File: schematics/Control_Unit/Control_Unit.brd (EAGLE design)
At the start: 58.4 x 65.4 mm, 144 parts, among them IC1 74HC174N, IC10 74HC74N, IC101 74HCT08N, IC103 74HC373N, IC104 74HCT08N, IC108 74HCT32N, IC11 74HC74N, IC110 74HCT32N, IC12 74AC08N, IC124 74HCT32N, IC125 74HCT08N, IC126 74AC157N, IC127 74HCT08N, IC128 74AC08N, IC129 74AC08N, IC13 74AC08N, IC130 74HCT04N, IC14 74HC74N, IC15 74HC74N, IC16 74AC08N, IC164 74HC174N, IC165 74HC174N, IC166 74HC174N, IC167 74HC174N, IC168 74HCT32N, IC169 74HCT32N, IC17 74HCT32N, IC172 74HCT32N, IC173 74HCT32N, IC174 74HCT32N, IC175 74HC193N, IC176 74HC193N, IC177 74HC193N, IC178 74HC193N, IC179 74HC193N, IC18 74AC08N, IC180 74HC193N, IC181 74HC193N, IC182 74HC193N, IC19 74AC08N, IC190 74HCT32N, IC191 74HCT32N, IC2 74HC174N, IC20 74AC08N, IC21 74AC08N, IC22 74HCT32N, IC23 74HCT08N, IC24 74HCT08N, IC25 74HCT32N, IC26 74HCT08N, IC27 74HCT08N, IC28 74HCT08N, IC29 74HCT08N, IC3 74HC151N, IC30 74HCT08N, IC31 74HCT04N, IC32 74HCT32N, IC33 74HCT32N, IC34 74HCT08N, IC35 74HCT04N, IC36 CY62256LL-PC, IC37 74HCT04N, IC38 74HCT08N, IC39 74HCT08N, IC4 74HC174N, IC40 74HCT32N, IC41 74HCT08N, IC42 74HC373N, IC43 74HCT04N, IC44 74HCT04N, IC45 74HCT04N, IC46 74ACT157N, IC47 74HCT04N, IC48 74HCT04N, IC49 74AC86N, IC5 74HC174N, IC50 74HC174N, IC51 74HCT32N, IC52 74HCT32N, IC53 74HCT32N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

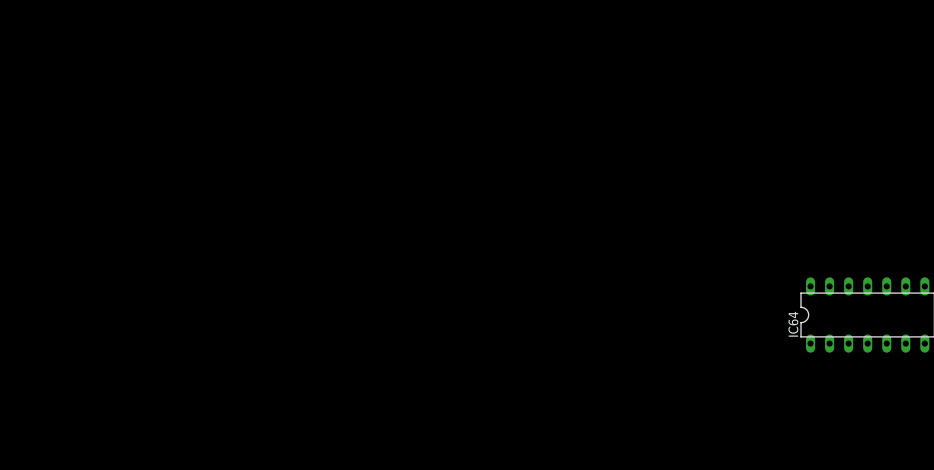
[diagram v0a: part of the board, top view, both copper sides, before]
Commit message: add second byte load of instruction fetch.
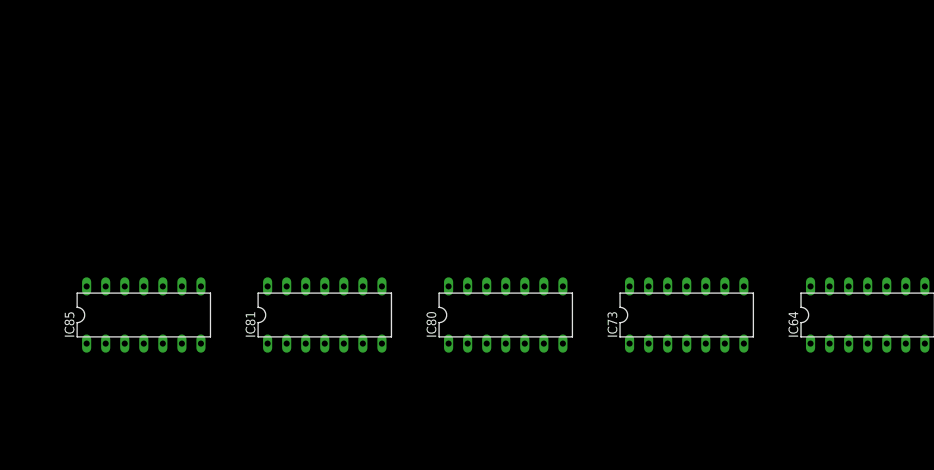
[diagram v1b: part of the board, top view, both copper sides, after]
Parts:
- added IC73, IC81: 74HCT08N, 74xx-eu:DIL14
- added IC80, IC85: 74HCT32N, 74xx-eu:DIL14
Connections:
- removed net IR_HIGH_LOAD_INPUT: IC4.9, IC5.9
- new net CLR_NOT_OE/CLR_NOT_CS_CYCL_2: IC80.11, IC85.2
- new net IR_LOAD_INPUT: IC4.9, IC5.9, IC80.12, IC81.11
- new net N$195: IC73.11, IC80.13
- new net N$200: IC63.13, IC85.3
- new net TWO_BYTE_CMD: IC73.12, IC81.13
- net CLR_NOT_CS_LDR: now also IC85.1; no longer IC63.13
- net CYCL_3: now also IC73.13
- net CYCL_4: now also IC81.12
- net GND: now also IC73.7, IC80.7, IC81.7, IC85.7
- net VCC: now also IC73.14, IC80.14, IC81.14, IC85.14
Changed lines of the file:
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@@
 <element name="IC31" library="74xx-eu" package="DIL14" value="74HCT04N" x="-63.1825" y="3.175"/>
 <element name="IC64" library="74xx-eu" package="DIL14" value="74HCT08N" x="-69.215" y="3.175"/>
+<element name="IC73" library="74xx-eu" package="DIL14" value="74HCT08N" x="-75.2475" y="3.175"/>
+<element name="IC80" library="74xx-eu" package="DIL14" value="74HCT32N" x="-81.28" y="3.175"/>
+<element name="IC81" library="74xx-eu" package="DIL14" value="74HCT08N" x="-87.3125" y="3.175"/>
+<element name="IC85" library="74xx-eu" package="DIL14" value="74HCT32N" x="-93.345" y="3.175"/>
 </elements>
 <signals>
@@
 <contactref element="IC31" pad="7"/>
 <contactref element="IC64" pad="7"/>
+<contactref element="IC73" pad="7"/>
+<contactref element="IC80" pad="7"/>
+<contactref element="IC81" pad="7"/>
+<contactref element="IC85" pad="7"/>
 <wire x1="52.3875" y1="58.1025" x2="49.8575" y2="63.5" width="0" layer="19" extent="1-1"/>
 <wire x1="51.435" y1="53.975" x2="52.3875" y2="58.1025" width="0" layer="19" extent="1-1"/>
@@
 <wire x1="-61.2775" y1="2.2225" x2="-49.2125" y2="2.2225" width="0" layer="19" extent="1-1"/>
 <wire x1="-67.31" y1="2.2225" x2="-61.2775" y2="2.2225" width="0" layer="19" extent="1-1"/>
+<wire x1="-73.3425" y1="2.2225" x2="-67.31" y2="2.2225" width="0" layer="19" extent="1-1"/>
+<wire x1="-79.375" y1="2.2225" x2="-73.3425" y2="2.2225" width="0" layer="19" extent="1-1"/>
+<wire x1="-85.4075" y1="2.2225" x2="-79.375" y2="2.2225" width="0" layer="19" extent="1-1"/>
+<wire x1="-91.44" y1="2.2225" x2="-85.4075" y2="2.2225" width="0" layer="19" extent="1-1"/>
 </signal>
 <signal name="VCC">
@@
 <contactref element="IC31" pad="14"/>
 <contactref element="IC64" pad="14"/>
+<contactref element="IC73" pad="14"/>
+<contactref element="IC80" pad="14"/>
+<contactref element="IC81" pad="14"/>
+<contactref element="IC85" pad="14"/>
 <wire x1="46.6725" y1="60.0075" x2="51.1075" y2="63.5" width="0" layer="19" extent="1-1"/>
 <wire x1="46.99" y1="55.88" x2="46.6725" y2="60.0075" width="0" layer="19" extent="1-1"/>
@@
 <wire x1="-65.0875" y1="4.1275" x2="-53.0225" y2="4.1275" width="0" layer="19" extent="1-1"/>
 <wire x1="-71.12" y1="4.1275" x2="-65.0875" y2="4.1275" width="0" layer="19" extent="1-1"/>
+<wire x1="-77.1525" y1="4.1275" x2="-71.12" y2="4.1275" width="0" layer="19" extent="1-1"/>
+<wire x1="-83.185" y1="4.1275" x2="-77.1525" y2="4.1275" width="0" layer="19" extent="1-1"/>
+<wire x1="-89.2175" y1="4.1275" x2="-83.185" y2="4.1275" width="0" layer="19" extent="1-1"/>
+<wire x1="-95.25" y1="4.1275" x2="-89.2175" y2="4.1275" width="0" layer="19" extent="1-1"/>
 </signal>
 <signal name="CLR_NOT_OE/CLR_NOT_CS_CYCL_0">
@@
 <contactref element="IC11" pad="5"/>
 <contactref element="IC11" pad="12"/>
-<wire x1="9.2075" y1="53.0225" x2="10.4775" y2="51.1175" width="0" layer="19" extent="1-1"/>
+<contactref element="IC73" pad="13"/>
+<wire x1="9.2075" y1="53.0225" x2="-76.5175" y2="4.1275" width="0" layer="19" extent="1-1"/>
+<wire x1="10.4775" y1="51.1175" x2="9.2075" y2="53.0225" width="0" layer="19" extent="1-1"/>
 </signal>
 <signal name="CYCL_5">
@@
 <contactref element="IC14" pad="2"/>
 <contactref element="IC11" pad="9"/>
-<wire x1="11.1125" y1="53.0225" x2="13.6525" y2="51.1175" width="0" layer="19" extent="1-1"/>
+<contactref element="IC81" pad="12"/>
+<wire x1="11.1125" y1="53.0225" x2="-87.9475" y2="4.1275" width="0" layer="19" extent="1-1"/>
+<wire x1="13.6525" y1="51.1175" x2="11.1125" y2="53.0225" width="0" layer="19" extent="1-1"/>
 </signal>
 <signal name="OPCODE_2">
@@
 <wire x1="5.3975" y1="41.5925" x2="25.7175" y2="24.4475" width="0" layer="19" extent="1-1"/>
 </signal>
-<signal name="IR_HIGH_LOAD_INPUT">
+<signal name="IR_LOAD_INPUT">
 <contactref element="IC4" pad="9"/>
 <contactref element="IC5" pad="9"/>
-<wire x1="13.0175" y1="37.7825" x2="18.7325" y2="37.7825" width="0" layer="19" extent="1-1"/>
+<contactref element="IC81" pad="11"/>
+<contactref element="IC80" pad="12"/>
+<wire x1="-81.915" y1="4.1275" x2="-87.3125" y2="4.1275" width="0" layer="19" extent="1-1"/>
+<wire x1="13.0175" y1="37.7825" x2="-81.915" y2="4.1275" width="0" layer="19" extent="1-1"/>
+<wire x1="18.7325" y1="37.7825" x2="13.0175" y2="37.7825" width="0" layer="19" extent="1-1"/>
 </signal>
 <signal name="REG_0_LOAD_INPUT">
@@
 </signal>
 <signal name="CLR_NOT_CS_LDR">
-<contactref element="IC63" pad="13"/>
 <contactref element="IC173" pad="1"/>
 <contactref element="IC173" pad="6"/>
+<contactref element="IC85" pad="1"/>
 <wire x1="38.4175" y1="58.7375" x2="41.5925" y2="58.7375" width="0" layer="19" extent="1-1"/>
-<wire x1="33.9725" y1="56.8325" x2="38.4175" y2="58.7375" width="0" layer="19" extent="1-1"/>
+<wire x1="-95.25" y1="2.2225" x2="38.4175" y2="58.7375" width="0" layer="19" extent="1-1"/>
 </signal>
 <signal name="CLR_NOT_CS_STR">
@@
 </signal>
 <signal name="N$126">
-<contactref element="IC17" pad="3"/>
 <contactref element="IC63" pad="12"/>
+<contactref element="IC17" pad="3"/>
 <wire x1="-3.4925" y1="2.2225" x2="34.6075" y2="56.8325" width="0" layer="19" extent="1-1"/>
 </signal>
@@
 <contactref element="IC20" pad="11"/>
 </signal>
+<signal name="TWO_BYTE_CMD">
+<contactref element="IC81" pad="13"/>
+<contactref element="IC73" pad="12"/>
+<wire x1="-75.8825" y1="4.1275" x2="-88.5825" y2="4.1275" width="0" layer="19" extent="1-1"/>
+</signal>
+<signal name="N$195">
+<contactref element="IC73" pad="11"/>
+<contactref element="IC80" pad="13"/>
+<wire x1="-75.2475" y1="4.1275" x2="-82.55" y2="4.1275" width="0" layer="19" extent="1-1"/>
+</signal>
+<signal name="CLR_NOT_OE/CLR_NOT_CS_CYCL_2">
+<contactref element="IC80" pad="11"/>
+<contactref element="IC85" pad="2"/>
+<wire x1="-81.28" y1="4.1275" x2="-94.615" y2="2.2225" width="0" layer="19" extent="1-1"/>
+</signal>
+<signal name="N$200">
+<contactref element="IC63" pad="13"/>
+<contactref element="IC85" pad="3"/>
+<wire x1="33.9725" y1="56.8325" x2="-93.98" y2="2.2225" width="0" layer="19" extent="1-1"/>
+</signal>
 </signals>

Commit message: reorder arguments. decoding is now easier
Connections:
- net INPUT_REG==OUTPUT_REG renamed INPUT_REG_IS_NOT_OUTPUT_REG
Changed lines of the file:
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@@
 <wire x1="9.2075" y1="43.4975" x2="3.4925" y2="49.2125" width="0" layer="19" extent="1-1"/>
 </signal>
-<signal name="INPUT_REG==OUTPUT_REG">
+<signal name="INPUT_REG_IS_NOT_OUTPUT_REG">
 <contactref element="IC168" pad="11"/>
 <contactref element="IC76" pad="1"/>

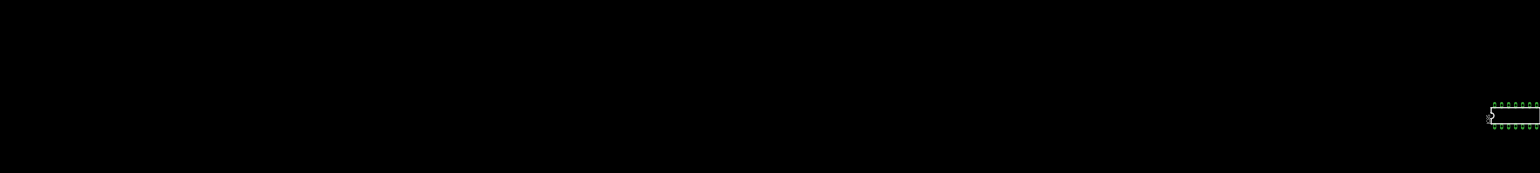
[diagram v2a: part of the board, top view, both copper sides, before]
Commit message: add two byte cmd decoder
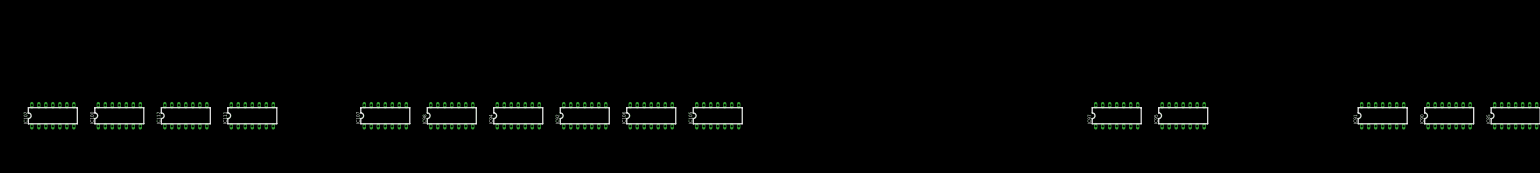
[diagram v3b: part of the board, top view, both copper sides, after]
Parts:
- added IC100, IC105, IC106, IC111, IC112, IC92, IC94, IC97, IC98: 74HCT32N, 74xx-eu:DIL14
- added IC102, IC107, IC90: 74HCT04N, 74xx-eu:DIL14
- added IC91, IC95: 74HCT08N, 74xx-eu:DIL14
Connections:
- removed net N$112: IC21.3, IC27.2, IC27.5, IC28.2
- removed net N$129: IC21.8, IC23.10, IC23.2, IC23.5
- removed net N$148: IC21.11, IC23.13, IC24.10, IC24.2, IC24.5
- removed net N$194: IC20.11
- new net LDR: IC112.12, IC21.3, IC27.2, IC27.5, IC28.2
- new net N$201: IC91.11, IC97.12
- new net N$203: IC95.11, IC97.13
- new net N$205: IC90.8, IC91.12
- new net N$206: IC102.8, IC91.13
- new net N$207: IC107.9, IC98.11
- new net N$213: IC94.11, IC98.13
- new net N$217: IC92.11, IC98.12
- new net N$218: IC100.13, IC105.11, IC95.12
- new net N$220: IC105.12, IC106.11
- new net N$227: IC107.8, IC95.13
- new net N$230: IC111.12, IC112.11
- new net POP: IC111.13, IC21.11, IC23.13, IC24.10, IC24.2, IC24.5
- new net PTR_ADD: IC101.10, IC104.10, IC104.13, IC104.2, IC106.13, IC124.4, IC127.5, IC20.6
- new net PUSH: IC105.13, IC21.8, IC23.10, IC23.2, IC23.5
- new net SAVE_LR/RET: IC112.13, IC20.11
- new net STR: IC106.12, IC21.6, IC27.10, IC27.13
- net GND: now also IC100.7, IC102.7, IC105.7, IC106.7, IC107.7, IC111.7, IC112.7, IC90.7, IC91.7, IC92.7, IC94.7, IC95.7, IC97.7, IC98.7
- net INPUT_REG_IS_NOT_OUTPUT_REG: now also IC90.9
- net N$13: now also IC100.12, IC111.11; no longer IC21.6, IC27.10, IC27.13
- net N$7: now also IC100.11, IC102.9; no longer IC101.10, IC104.10, IC104.13, IC104.2, IC124.4, IC127.5, IC20.6
- net OPCODE_4: now also IC92.12
- net OPCODE_5: now also IC94.12
- net OPCODE_6: now also IC92.13
- net OPCODE_7: now also IC94.13
- net TWO_BYTE_CMD: now also IC97.11
- net VCC: now also IC100.14, IC102.14, IC105.14, IC106.14, IC107.14, IC111.14, IC112.14, IC90.14, IC91.14, IC92.14, IC94.14, IC95.14, IC97.14, IC98.14

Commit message: implement SAVE_LR/RET structure. LR register needs to be added.
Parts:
- removed IC102: 74HCT04N, 74xx-eu:DIL14
- removed IC105, IC106, IC111, IC174, IC92, IC94, IC97, IC98: 74HCT32N, 74xx-eu:DIL14
- removed IC95: 74HCT08N, 74xx-eu:DIL14
- added IC109: 74HCT08N, 74xx-eu:DIL14
- added IC117: 74HC74N, 74xx-eu:DIL14
- IC29: value 74HCT08N -> 74HCT32N
- IC31, IC48: value 74HCT04N -> 74HCT32N
- IC51, IC53: value 74HCT32N -> 74HCT08N
- IC90: value 74HCT04N -> 74HCT08N
- moved IC29 302.2 mm to (-268.3, 3.17)
- moved IC48 265.4 mm to (-280.4, 3.17)
- moved IC51 265.4 mm to (-286.4, 3.17)
- moved IC53 265.4 mm to (-292.4, 3.17)
- moved IC70 247.3 mm to (-298.4, 3.17)
- moved IC73 229.2 mm to (-304.5, 3.17)
- moved IC85 223.2 mm to (-316.5, 3.17)
- moved IC81 223.2 mm to (-310.5, 3.17)
- moved IC90 223.2 mm to (-322.6, 3.17)
- moved IC31 211.1 mm to (-274.3, 3.17)
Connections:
- net CYCL6 renamed CYCL_6
- net TABLE_B_INPUT_BR_HIGH renamed TABLE_B_INPUT_PTR_HIGH
- new net CYCL_0: IC10.12, IC10.5, IC80.5
- new net CYCL_10: IC10.2, IC117.9
- new net CYCL_8: IC117.2, IC15.9
- new net CYCL_9: IC117.12, IC117.5
- new net N$112: IC109.3, IC29.2
- new net N$129: IC109.10, IC130.10
- new net N$194: IC109.11, IC109.2, IC73.2, IC81.5, IC90.5
- new net N$219: IC109.5, IC109.8, IC51.2, IC53.5, IC70.5
- new net N$223: IC109.6, IC31.2
- new net N$224: IC85.1, IC90.6
- new net N$225: IC31.3
- new net N$226: IC48.2, IC53.6
- new net N$228: IC48.1, IC70.6
- new net N$229: IC29.1, IC73.3
- new net N$231: IC48.3
- new net N$232: IC85.3
- new net N$233: IC81.6, IC85.2
- new net WRITE_LR_DBUS_SAVE_LR: IC29.3
- net CLR_NOT_CS_LDR: now also IC17.4; no longer IC85.1
- net CLR_NOT_OE/CLR_NOT_CS_CYCL_0: now also IC80.6; no longer IC51.11
- net CLR_NOT_OE/CLR_NOT_CS_CYCL_2: now also IC17.5; no longer IC85.2
- net CYCL_3: now also IC91.5; no longer IC73.13
- net CYCL_4: now also IC91.1; no longer IC81.12
- net CYCL_7: now also IC15.12; no longer IC10.2
- net GND: now also IC109.7, IC117.7; no longer IC102.7, IC105.7, IC106.7, IC111.7, IC174.7, IC92.7, IC94.7, IC95.7, IC97.7, IC98.7
- net INPUT_REG_IS_NOT_OUTPUT_REG: now also IC107.11; no longer IC90.9
- net IR_LOAD_INPUT: now also IC91.3; no longer IC81.11
- net N$100: now also IC99.11; no longer IC53.3
- net N$118: now also IC124.12; no longer IC174.4
- net N$13: now also IC112.3; no longer IC111.11
- net N$132: now also IC125.6; no longer IC70.8
- net N$149: now also IC125.13, IC130.4; no longer IC29.10, IC31.2
- net N$15: now also IC125.11; no longer IC29.8
- net N$163: now also IC31.1, IC51.3; no longer IC10.12, IC10.5, IC51.13
- net N$168: now also IC99.13; no longer IC53.2
- net N$195: now also IC91.6; no longer IC73.11
- net N$197: now also IC124.11; no longer IC174.6
- net N$200: now also IC17.6; no longer IC85.3
- net N$201: now also IC80.1; no longer IC97.12
- net N$203: now also IC80.2, IC91.8; no longer IC95.11, IC97.13
- net N$205: now also IC107.10; no longer IC90.8
- net N$206: now also IC107.2; no longer IC102.8
- net N$207: now also IC100.8; no longer IC98.11
- net N$213: now also IC100.10, IC100.3; no longer IC94.11, IC98.13
- net N$217: now also IC100.6, IC100.9; no longer IC92.11, IC98.12
- net N$218: now also IC112.8, IC91.9; no longer IC105.11, IC95.12
- net N$22: now also IC125.5, IC130.3; no longer IC31.1, IC70.10
- net N$220: now also IC112.6, IC112.9; no longer IC105.12, IC106.11
- net N$227: now also IC91.10; no longer IC95.13
- net N$230: now also IC112.1; no longer IC111.12
- net N$31: now also IC37.1; no longer IC48.13
- net N$34: now also IC124.13; no longer IC174.5
- net N$69: now also IC37.2; no longer IC48.12
- net N$7: now also IC107.1; no longer IC102.9
- net N$82: now also IC125.12, IC125.4; no longer IC29.9, IC70.9
- net OPCODE_4: now also IC100.4; no longer IC92.12
- net OPCODE_5: now also IC100.1, IC109.12, IC130.11; no longer IC94.12
- net OPCODE_6: now also IC100.5; no longer IC92.13
- net OPCODE_7: now also IC100.2; no longer IC94.13
- net OPCODE_LOAD_INPUT: now also IC80.4; no longer IC51.12
- net PC_COUNT_UP_FETCH1: now also IC99.12; no longer IC53.1
- net POP: now also IC112.2; no longer IC111.13
- net PTR_ADD: now also IC112.5; no longer IC106.13
- net PUSH: now also IC112.10; no longer IC105.13
- net RING_CNTR_CLOCK: now also IC117.11, IC117.3, IC15.11
- net RING_CNTR_CLR: now also IC117.1, IC117.13, IC15.13
- net SAVE_LR/RET: now also IC109.13, IC109.9
- net STATE_1: now also IC109.1, IC109.4
- net STATE_2: now also IC51.1, IC73.1
- net STATE_3: now also IC53.4, IC81.4
- net STATE_4: now also IC70.4, IC90.4
- net STR: now also IC112.4; no longer IC106.12
- net TWO_BYTE_CMD: now also IC80.3, IC91.2, IC91.4; no longer IC73.12, IC81.13, IC97.11
- net VCC: now also IC109.14, IC117.14; no longer IC102.14, IC105.14, IC106.14, IC111.14, IC174.14, IC92.14, IC94.14, IC95.14, IC97.14, IC98.14

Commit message: add LR register. All instructions are now implemented.
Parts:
- added IC102, IC105, IC106, IC111, IC113, IC114, IC115, IC98: 74HC151N, 74xx-eu:DIL16
- added IC116: 74HC373N, 74xx-eu:DIL20
- added IC118, IC119, IC134, IC135, IC136, IC137, IC139, IC140: 74HCT08N, 74xx-eu:DIL14
- added IC120, IC121, IC122, IC123, IC131, IC132, IC133, IC138: 74HCT04N, 74xx-eu:DIL14
- added IC141, IC142, IC143, IC144, IC145, IC146, IC147, IC148: 74HCT32N, 74xx-eu:DIL14
- added IC92, IC94, IC95, IC97: 74HC174N, 74xx-eu:DIL16
- moved IC90 337.9 mm to (15.2, 11.7), turned to 180 degrees
- moved IC85 321.4 mm to (4.76, 8.89), turned to 180 degrees
- moved IC81 320.4 mm to (9.84, 8.89), turned to 180 degrees
- moved IC73 319.8 mm to (15.2, 8.89), turned to 180 degrees
- moved IC70 318.8 mm to (20.3, 8.57), turned to 180 degrees
- moved IC53 318.2 mm to (25.7, 8.89), turned to 180 degrees
- moved IC51 317.5 mm to (31.1, 8.57), turned to 180 degrees
- moved IC48 316.6 mm to (36.2, 9.21), turned to 180 degrees
- moved IC31 279.1 mm to (4.76, 6.03), turned to 180 degrees
- moved IC29 278.1 mm to (9.84, 6.35), turned to 180 degrees
- moved IC117 272.5 mm to (10.2, 11.7)
- moved IC109 252.9 mm to (20.6, 11.4)
- moved IC100 246.2 mm to (26.0, 11.4)
- moved IC112 245.6 mm to (31.4, 11.4)
- moved IC107 233.2 mm to (37.1, 12.1)
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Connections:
- net IO_OUTPUT_REG_1 renamed IO_OUTPUT_REG_1_LOAD_INPUT
- net IO_OUTPUT_REG_2 renamed IO_OUTPUT_REG_2_LOAD_INPUT
- net TABLE_B_INPUT_PTR_HIGH renamed TABLE_1_INPUT_PTR_HIGH
- net TABLE_B_INPUT_PTR_L renamed TABLE_1_INPUT_PTR_L
- net TABLE_B_INPUT_REG0 renamed TABLE_1_INPUT_REG0
- net TABLE_B_INPUT_REG1 renamed TABLE_1_INPUT_REG1
- net TABLE_B_INPUT_REG2 renamed TABLE_1_INPUT_REG2
- net TABLE_B_INPUT_REG3 renamed TABLE_1_INPUT_REG3
- removed net FSDFAFSDFSFDDDDDDDDDDDDDDDDDDDDDDDDDDDDDDDD: IC34.3, IC39.10, IC39.2, IC41.10, IC41.2
- removed net N$225: IC31.3
- removed net N$228: IC48.1, IC70.6
- removed net N$229: IC29.1, IC73.3
- removed net N$231: IC48.3
- removed net N$232: IC85.3
- removed net PC_HIGH_LOAD_INPUT_NOT: IC181.11, IC182.11, IC43.8
- removed net PC_LOW_LOAD_INPUT_NOT: IC179.11, IC180.11, IC43.6
- removed net PTR_L_LOAD_INPUT_NOT: IC1.9, IC2.9, IC43.2
- removed net WRITE_LR_DBUS_SAVE_LR: IC29.3
- new net DATA10: IC116.6
- new net DATA11: IC116.9
- new net DATA12: IC116.12
- new net DATA13: IC116.15
- new net DATA14: IC116.16
- new net DATA15: IC116.19
- new net DATA8: IC116.2
- new net DATA9: IC116.5
- new net FILL_LR_H_SAVE_LR: IC146.4, IC85.1, IC90.6
- new net FILL_LR_L_SAVE_LR: IC145.4, IC29.1, IC73.3
- new net FILL_PC_H_RET: IC147.5, IC48.1, IC70.6
- new net FILL_PC_L_RET: IC148.5, IC31.1, IC51.3
- new net FSDFAFSDFSFDDDDDDDDDDDDDDDDDDDDDDDDDDDDDDDD1: IC137.3, IC39.10, IC39.2, IC41.10, IC41.2
- new net LR_DATA_OUT_0: IC115.4, IC92.2
- new net LR_DATA_OUT_1: IC114.4, IC92.5
- new net LR_DATA_OUT_10: IC113.3, IC95.7
- new net LR_DATA_OUT_11: IC111.3, IC95.10
- new net LR_DATA_OUT_12: IC106.3, IC95.12
- new net LR_DATA_OUT_13: IC105.3, IC95.15
- new net LR_DATA_OUT_14: IC97.2, IC98.3
- new net LR_DATA_OUT_15: IC102.3, IC97.5
- new net LR_DATA_OUT_2: IC113.4, IC92.7
- new net LR_DATA_OUT_3: IC111.4, IC92.10
- new net LR_DATA_OUT_4: IC106.4, IC92.12
- new net LR_DATA_OUT_5: IC105.4, IC92.15
- new net LR_DATA_OUT_6: IC94.2, IC98.4
- new net LR_DATA_OUT_7: IC102.4, IC94.5
- new net LR_DATA_OUT_8: IC115.3, IC95.2
- new net LR_DATA_OUT_9: IC114.3, IC95.5
- new net LR_H_LOAD_INPUT: IC123.3, IC146.6
- new net LR_H_LOAD_INPUT_TABLE_1: IC135.6, IC146.5
- new net LR_L_LOAD_INPUT: IC122.3, IC145.6
- new net LR_L_LOAD_INPUT_TABLE_1: IC135.3, IC145.5
- new net N$167: IC123.4, IC95.9, IC97.9
- new net N$234: IC122.4, IC92.9, IC94.9
- new net N$235: IC134.13, IC134.5, IC135.13, IC135.5, IC139.3
- new net N$239: IC134.10, IC134.2, IC135.10, IC135.2, IC140.3
- new net N$247: IC138.10, IC139.2, IC140.2
- new net N$248: IC141.3, IC143.1
- new net N$249: IC142.3, IC143.2
- new net N$250: IC143.3, IC144.2
- new net N$252: IC144.3, IC25.10
- new net N$258: IC115.5, IC116.3
- new net N$259: IC114.5, IC116.4
- new net N$260: IC113.5, IC116.7
- new net N$261: IC111.5, IC116.8
- new net N$262: IC106.5, IC116.13
- new net N$263: IC105.5, IC116.14
- new net N$264: IC116.17, IC98.5
- new net N$265: IC102.5, IC116.18
- new net N$266: IC118.13, IC119.13, IC25.8
- new net N$267: IC116.11, IC119.11, IC121.9
- new net N$268: IC118.12, IC120.8
- new net N$269: IC116.1, IC121.8
- new net NOT_USED0: IC135.8
- new net NOT_USED05: IC134.11
- new net NOT_USED1: IC135.11
- new net NOT_USED2: IC134.3
- new net NOT_USED3: IC134.6
- new net NOT_USED4: IC134.8
- new net PC_HIGH_LOAD_INPUT: IC132.5, IC147.6
- new net PC_LOW_LOAD_INPUT: IC133.9, IC84.6
- new net PTR_L_LOAD_INPUT: IC131.5, IC169.8
- new net REGISTER_OUTPUT_SEL_3: IC119.12, IC120.9, IC46.12
- new net UNNAME: IC133.8, IC179.11, IC180.11
- new net WRITE_LR_H_DBUS_RET: IC141.2, IC48.3
- new net WRITE_LR_L_DBUS_RET: IC141.1, IC31.3
- new net WRITE_PC_H_DBUS_SAVE_LR: IC142.2, IC85.3
- new net WRITE_PC_L_DBUS_SAVE_LR: IC142.1, IC29.3
- net DATA0: now also IC92.3, IC95.3
- net DATA1: now also IC92.4, IC95.4
- net DATA2: now also IC92.6, IC95.6
- net DATA3: now also IC92.11, IC95.11
- net DATA4: now also IC92.13, IC95.13
- net DATA5: now also IC92.14, IC95.14
- net DATA6: now also IC94.3, IC97.3
- net DATA7: now also IC94.4, IC97.4
- net DATA_BUS_ENABLE_LATCH: now also IC118.11; no longer IC25.8
- net FILL_PC_L_JMP_O: now also IC148.4; no longer IC84.5
- net GND: now also IC102.7, IC102.8, IC105.7, IC105.8, IC106.7, IC106.8, IC111.7, IC111.8, IC113.7, IC113.8, IC114.7, IC114.8, IC115.7, IC115.8, IC116.10, IC118.7, IC119.7, IC120.7, IC121.7, IC122.7, IC123.7, IC131.7, IC132.7, IC133.7, IC134.7, IC135.7, IC136.7, IC137.7, IC138.7, IC139.7, IC140.7, IC141.7, IC142.7, IC143.7, IC144.7, IC145.7, IC146.7, IC147.7, IC148.7, IC92.1, IC92.8, IC94.1, IC94.11, IC94.13, IC94.14, IC94.6, IC94.8, IC95.1, IC95.8, IC97.1, IC97.11, IC97.13, IC97.14, IC97.6, IC97.8, IC98.7, IC98.8; no longer IC46.13
- net INPUT_REG0: now also IC135.1, IC135.4
- net INPUT_REG1: now also IC135.12, IC135.9
- net INPUT_REG2: now also IC134.1, IC134.4
- net INPUT_REG3: now also IC134.12, IC134.9
- net N$136: now also IC136.3, IC39.13, IC39.5, IC41.13, IC41.5; no longer IC43.5, IC84.6
- net N$163: now also IC148.6, IC84.5; no longer IC31.1, IC51.3
- net N$18: now also IC137.2, IC140.1, IC34.3; no longer IC34.6, IC39.13, IC39.5, IC41.13, IC41.5
- net N$224: now also IC136.2, IC139.1, IC34.6; no longer IC85.1, IC90.6
- net N$72: now also IC1.9, IC131.6, IC2.9; no longer IC169.6, IC43.3
- net N$73: now also IC132.6, IC181.11, IC182.11; no longer IC169.8, IC43.1
- net N$90: now also IC144.1; no longer IC25.10
- net OPCODE_7: now also IC136.1, IC137.1, IC138.11, IC46.13
- net PC_DATA_OUT_0: now also IC115.2
- net PC_DATA_OUT_1: now also IC114.2
- net PC_DATA_OUT_10: now also IC113.1
- net PC_DATA_OUT_11: now also IC111.1
- net PC_DATA_OUT_12: now also IC106.1
- net PC_DATA_OUT_13: now also IC105.1
- net PC_DATA_OUT_14: now also IC98.1
- net PC_DATA_OUT_15: now also IC102.1
- net PC_DATA_OUT_2: now also IC113.2
- net PC_DATA_OUT_3: now also IC111.2
- net PC_DATA_OUT_4: now also IC106.2
- net PC_DATA_OUT_5: now also IC105.2
- net PC_DATA_OUT_6: now also IC98.2
- net PC_DATA_OUT_7: now also IC102.2
- net PC_DATA_OUT_8: now also IC115.1
- net PC_DATA_OUT_9: now also IC114.1
- net PC_HIGH_LOAD_INPUT_JMP: now also IC147.4; no longer IC43.9
- net PTR_H_LOAD_INPUT_NOT: now also IC169.6; no longer IC43.4
- net REGISTER_OUTPUT_SEL_0: now also IC102.11, IC105.11, IC106.11, IC111.11, IC113.11, IC114.11, IC115.11, IC98.11
- net REGISTER_OUTPUT_SEL_1: now also IC102.10, IC105.10, IC106.10, IC111.10, IC113.10, IC114.10, IC115.10, IC98.10
- net REGISTER_OUTPUT_SEL_2: now also IC102.9, IC105.9, IC106.9, IC111.9, IC113.9, IC114.9, IC115.9, IC98.9
- net VCC: now also IC102.16, IC105.16, IC106.16, IC111.16, IC113.16, IC114.16, IC115.16, IC116.20, IC118.14, IC119.14, IC120.14, IC121.14, IC122.14, IC123.14, IC131.14, IC132.14, IC133.14, IC134.14, IC135.14, IC136.14, IC137.14, IC138.14, IC139.14, IC140.14, IC141.14, IC142.14, IC143.14, IC144.14, IC145.14, IC146.14, IC147.14, IC148.14, IC92.16, IC94.16, IC95.16, IC97.16, IC98.16
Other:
- board size 58.4 x 65.4 mm -> 58.4 x 86.3 mm
